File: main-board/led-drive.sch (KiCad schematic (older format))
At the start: 8 parts

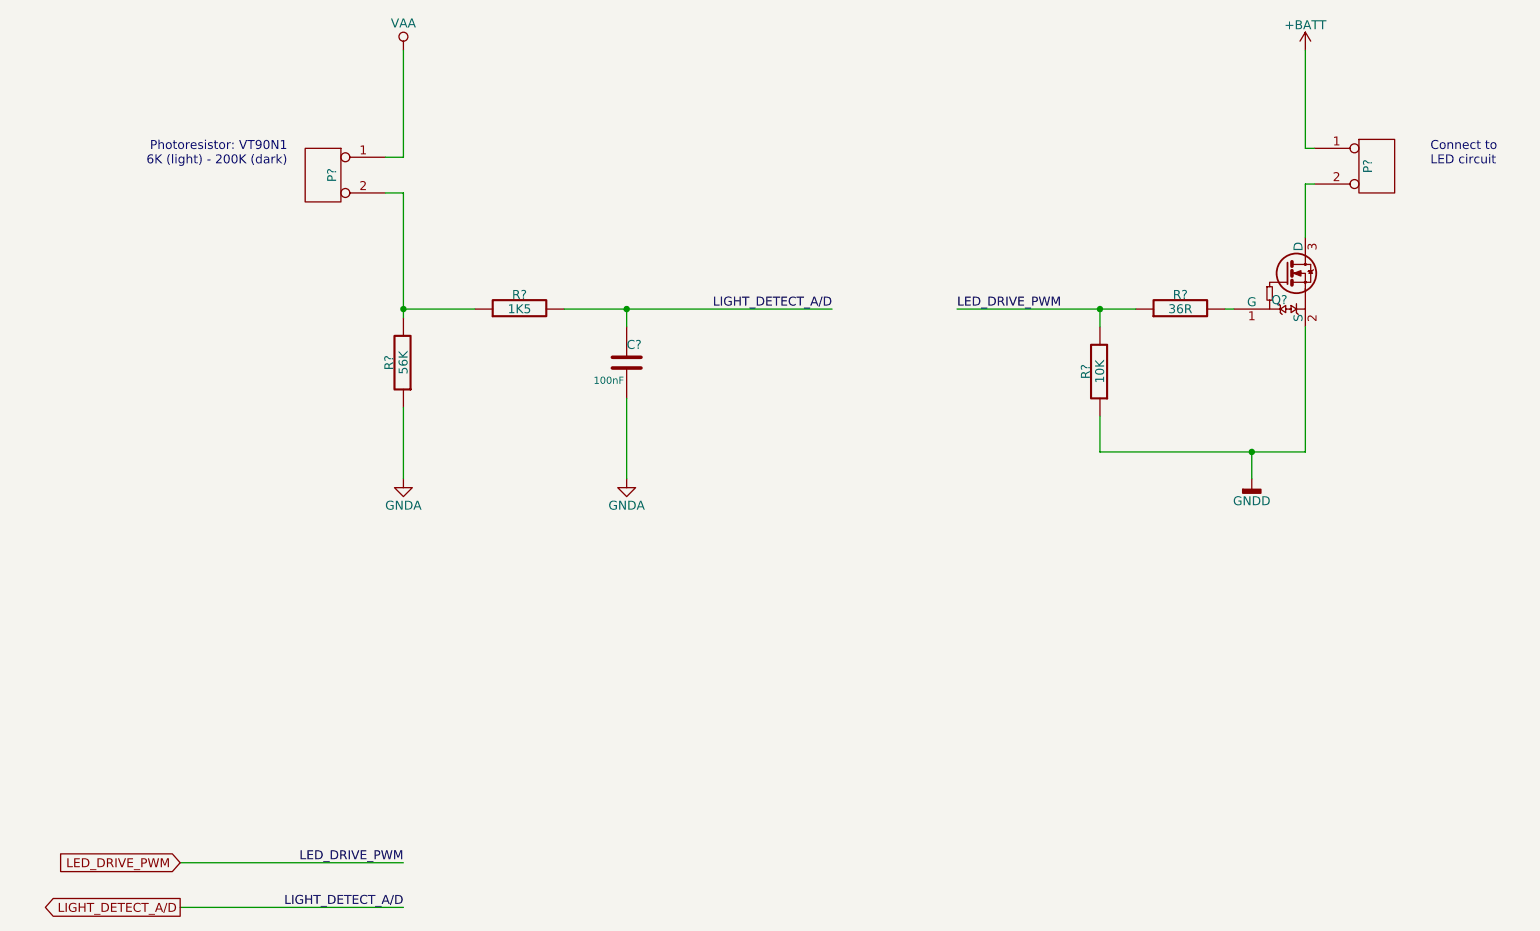
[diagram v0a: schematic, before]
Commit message: Added output files, gerbers, dril files, raster images, and updates to PCB design files.
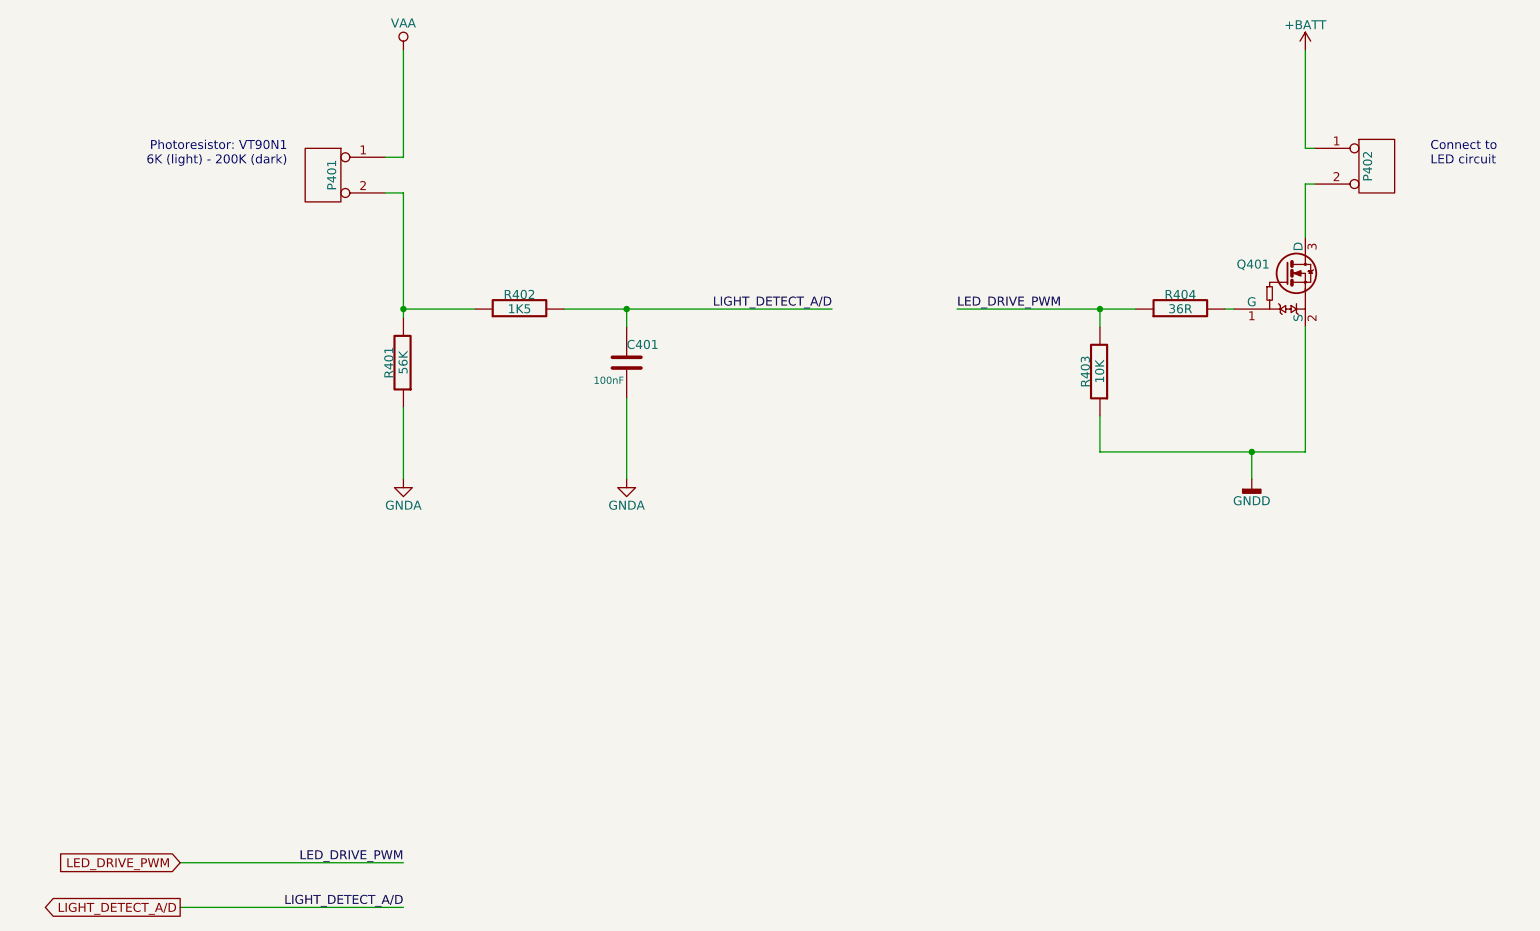
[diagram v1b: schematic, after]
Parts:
- gave numbers to parts that had none: 8
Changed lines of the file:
@@
 $Descr A4 11693 8268
 encoding utf-8
-Sheet 2 4
+Sheet 4 4
 Title "Main Board"
 Date "2020-04-24"
@@
 LED_DRIVE_PWM
 $Comp
-L power:+BATT #PWR?
+L power:+BATT #PWR0405
 U 1 1 53A6B05B
 P 8450 2250
-F 0 "#PWR?" H 8450 2200 20  0001 C CNN
+F 0 "#PWR0405" H 8450 2200 20  0001 C CNN
 F 1 "+BATT" H 8450 2390 50  0000 C CNN
 F 2 "" H 8450 2250 50  0001 C CNN
@@
 Connection ~ 4650 3700
 $Comp
-L power:VAA #PWR?
+L power:VAA #PWR0401
 U 1 1 53ADFECC
 P 3400 2250
-F 0 "#PWR?" H 3400 2310 30  0001 C CNN
+F 0 "#PWR0401" H 3400 2310 30  0001 C CNN
 F 1 "VAA" H 3400 2400 50  0000 C CNN
 F 2 "" H 3400 2250 50  0001 C CNN
@@
 $EndComp
 $Comp
-L power:GNDA #PWR?
+L power:GNDA #PWR0402
 U 1 1 53AE09B6
 P 3400 4650
-F 0 "#PWR?" H 3400 4650 50  0001 C CNN
+F 0 "#PWR0402" H 3400 4650 50  0001 C CNN
 F 1 "GNDA" H 3400 4500 50  0000 C CNN
 F 2 "" H 3400 4650 50  0001 C CNN
@@
 $EndComp
 $Comp
-L power:GNDD #PWR?
+L power:GNDD #PWR0404
 U 1 1 53AE09BE
 P 8150 4650
-F 0 "#PWR?" H 8150 4650 50  0001 C CNN
+F 0 "#PWR0404" H 8150 4650 50  0001 C CNN
 F 1 "GNDD" H 8150 4525 50  0000 C CNN
 F 2 "" H 8150 4650 50  0001 C CNN
@@
 Photoresistor: VT90N1\n6K (light) - 200K (dark)
 $Comp
-L power:GNDA #PWR?
+L power:GNDA #PWR0403
 U 1 1 53B231BE
 P 4650 4650
-F 0 "#PWR?" H 4650 4650 50  0001 C CNN
+F 0 "#PWR0403" H 4650 4650 50  0001 C CNN
 F 1 "GNDA" H 4650 4500 50  0000 C CNN
 F 2 "" H 4650 4650 50  0001 C CNN
@@
 $EndComp
 $Comp
-L Connectors:ECS00067 P?
+L Connectors:ECS00067 P401
 U 1 1 53B8DD64
 P 2950 2950
-F 0 "P?" V 2900 2950 50  0000 C CNN
+F 0 "P401" V 2900 2950 50  0000 C CNN
 F 1 "ECS00067" H 2950 2700 50  0001 C CNN
 F 2 "ECFootprints:ECS00067F" H 2800 2850 50  0001 C CNN
@@
 $EndComp
 $Comp
-L Resistors:ECS00085 R?
+L Resistors:ECS00085 R401
 U 1 1 53B8DDA8
 P 3400 4000
-F 0 "R?" H 3400 4080 50  0000 C CNN
+F 0 "R401" H 3400 4080 50  0000 C CNN
 F 1 "ECS00085" H 3400 4250 50  0001 C CNN
 F 2 "ECFootprints:EC0603" H 3400 3930 30  0001 C CNN
@@
 $EndComp
 $Comp
-L Resistors:ECS00045 R?
+L Resistors:ECS00045 R403
 U 1 1 53B8DE1E
 P 7300 4050
-F 0 "R?" H 7300 4130 50  0000 C CNN
+F 0 "R403" H 7300 4130 50  0000 C CNN
 F 1 "ECS00045" H 7300 4300 50  0001 C CNN
 F 2 "ECFootprints:EC0603" H 7300 3980 30  0001 C CNN
@@
 $EndComp
 $Comp
-L Capacitors:ECS00075 C?
+L Capacitors:ECS00075 C401
 U 1 1 53B8DE4F
 P 4650 4000
-F 0 "C?" H 4650 4100 50  0000 L CNN
+F 0 "C401" H 4650 4100 50  0000 L CNN
 F 1 "ECS00075" V 4400 3850 40  0001 L CNN
 F 2 "ECFootprints:EC0603_C" H 4688 3850 30  0001 C CNN
@@
 $EndComp
 $Comp
-L Connectors:ECS00067 P?
+L Connectors:ECS00067 P402
 U 1 1 53B8DED5
 P 8850 2900
-F 0 "P?" V 8800 2900 50  0000 C CNN
+F 0 "P402" V 8800 2900 50  0000 C CNN
 F 1 "ECS00067" H 8850 2650 50  0001 C CNN
 F 2 "ECFootprints:ECS00067F" H 8700 2800 50  0001 C CNN
@@
 $EndComp
 $Comp
-L Transistors:ECS00087 Q?
+L Transistors:ECS00087 Q401
 U 1 1 53B8DEFB
 P 8350 3550
-F 0 "Q?" H 8350 3451 50  0000 R CNN
+F 0 "Q401" H 8250 3650 50  0000 R CNN
 F 1 "ECS00087" H 8200 3700 50  0001 R CNN
 F 2 "ECFootprints:ECSOT416" H 8220 3702 50  0001 C CNN
@@
 Connection ~ 3400 3700
 $Comp
-L Resistors:ECS00083 R?
+L Resistors:ECS00083 R402
 U 1 1 53D2EA70
 P 4050 3700
-F 0 "R?" H 4050 3780 50  0000 C CNN
+F 0 "R402" H 4050 3780 50  0000 C CNN
 F 1 "ECS00083" H 4050 3950 50  0001 C CNN
 F 2 "ECFootprints:EC0603" H 4050 3630 30  0001 C CNN
@@
 	4300 3700 4650 3700
 $Comp
-L Resistors:ECS00080 R?
+L Resistors:ECS00080 R404
 U 1 1 53D76744
 P 7750 3700
-F 0 "R?" H 7750 3780 50  0000 C CNN
+F 0 "R404" H 7750 3780 50  0000 C CNN
 F 1 "ECS00080" H 7750 3950 50  0001 C CNN
 F 2 "ECFootprints:EC0603" H 7750 3630 30  0001 C CNN
